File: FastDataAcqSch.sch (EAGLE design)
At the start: 94 parts, among them IC1 FT230XQ, J1 USB_MICROAB_SMT, X1 SMA-SMDRA, X2 87832-14, Y1 SI530-500

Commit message: Update 9/2/13
Added more ICs
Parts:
- added C62, C64, C66, C68: .1uF, Schuyler:CAPACITOR0204_REVERSE
- added C63, C65: 10nF, rcl:C-EUC0201
- added C67: 100pF, rcl:C-EUC0603
- added C69: 4.7uF, Schuyler:CAPACITOR0304_REVERSE
- added R19, R20, R24, R25: 10k, rcl:R-US_R0201
- added R21: 1k, rcl:R-US_0204/2V
- added R22: 83, rcl:R-US_0204/2V
- added R23: 130, rcl:R-US_0204/2V
- added U$6: TMP421, Schuyler:TMP421
- added U$7: DAC101C081, Schuyler:DAC101C081
- added Y2: DNP, Schuyler:SI500S
- added Y3: 100MHz, Schuyler:DS1088L_100MHZ
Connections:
- new net FPGA_CLK1: U$2.IO_L30N_GCLK0_USERCCLK_2, Y3.OUT
- new net FPGA_CLK2: U$2.IO_L31P_GCLK31_D14_2, Y2.OUTPUT
- new net FPGA_SCL: R19.1, R24.1, U$2.IO_L62N_D6_2, U$6.SCL, U$7.SCL
- new net FPGA_SDA: R20.1, R25.1, U$6.SDA, U$7.SDA
- new net FPGA_SDL: U$2.IO_L62P_D5_2
- new net N$10: R21.1
- new net N$9: R21.2, R22.2, R23.1
- new net VCC: R23.2
- net 3V3: now also C62.1, C63.1, C64.1, C65.1, C66.1, C68.1, C69.1, R19.2, R20.2, R24.2, R25.2, U$6.V+, U$7.VA, Y2.OE, Y2.VDD, Y3.!PDN, Y3.VCC@1, Y3.VCC@2
- net ADC_TDIODE+: now also C67.1, U$6.DXP
- net ADC_TDIODE-: now also C67.2, U$6.DXN
- net AGND: now also R22.1
- net DGND: now also C62.2, C63.2, C64.2, C65.2, C66.2, C68.2, C69.2, U$6.A0, U$6.A1, U$6.GND, U$7.ADR0, U$7.GND, Y2.GDN, Y3.GND@1, Y3.GND@2
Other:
- note added: "+"
- note added: "-"
- note added: "FPGA"
- note added: "FPGA Clock"
- note added: "Half of the differential output/differential latch input"
- note added: "Input Trigger"
- note added: "L"
- note added: "NOTE: C is 0603 so it can be changed"
- note added: "NOTE: Device address is: 1001 100"
- note added: "NOTE: Route CLK as 50 ohm impedance line. Termination described in datasheet."
- note added: "NOTE: Y3 is the primary clock. Y2 is a backup but should not be populated"
- note added: "Q"
- note added: "Temperature Sensor"
- note added: "Trigger"
- note added: "Trigger In"
- note added: "Trigger Reset"
- note added: "USB/UART Interface"
- note added: "Vref"
- note removed: "NOTE: Route CLK as 50 ohm impedance line."

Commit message: Nearly finalized schematic
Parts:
- removed R21: 1k, rcl:R-US_0204/2V
- removed R22: 83, rcl:R-US_0204/2V
- removed R23: 130, rcl:R-US_0204/2V
- removed R9: NA, rcl:R-US_R0603
- added C70, C71, C72, C73, C74, C75, C76, C77, C78, C97, C98, C99: 10uF, rcl:C-EUC0603
- added C79, C80, C81, C82, C83, C84, C85, C93: 33uF, SparkFun-Passives:CAP0805
- added C86, C87, C88, C89, C90, C91: 10pF, rcl:C-EUC0201
- added C92: 10nF, rcl:C-EUC0201
- added C94, C95, C96: 22uF 150mOhm ESR, rcl:C-USC0805
- added IC2: LT1963AEQ, linear-technology:LT1963AEQ
- added JP1: (no value), SparkFun-Passives:JUMPER-2PTH
- added L10, L11: 2.2uH, Schuyler:INDUCTOR_5.18X5.49
- added L6, L7, L8, L9: 2.2uH, Schuyler:INDUCTOR_3X3.6
- added R26, R27, R28, R29, R30, R31, R32, R33, R34, R35, R36, R37, R38, R41, R42, R43, R44, R45, R47, R48, R49: (no value), rcl:R-US_R0201
- added R39: 4.7k, rcl:R-US_R0201
- added R40: 0, rcl:R-US_R0603
- added R46, R50: (no value), rcl:R-US_R0603
- added R51: 10k, rcl:R-US_R0201
- added TP1, TP2, TP3, TP4, TP5, TP6, TP7, TP8, TP9: TPPAD1-13, testpad:TPPAD1-13
- added U$10: LT1963AEST-3.3, Schuyler:LT1963AEST-3.3
- added U$8: LTC3374QFN, Schuyler:LTC3374QFN
- added U$9: LT1963AEST-2.5, Schuyler:LT1963AEST-2.5
- R1: device rcl:R-US_R0402 -> rcl:R-US_R0201; MANPARTNUMBER (none) -> RC0603F49R9C; MANUFACTURER (none) -> Samsung Electro-Mechanics America, Inc; PARTNUMBER (none) -> 1276-3590-1-ND; SUPPLIER (none) -> DIGIKEY
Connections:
- removed net FGPA_PROGRAMB: U$2.PROGRAM_B_2
- removed net N$10: R21.1
- removed net N$9: R21.2, R22.2, R23.1
- new net 2V3_1V9PRE: C82.1, C89.1, C97.1, IC2.!SHDN, IC2.IN, L10.P$2, R32.2, TP3.TP
- new net 2V8_2V5PRE: C80.1, C91.1, C98.1, L9.P$2, R36.2, R48.2, TP1.TP, U$9.IN
- new net 3V3A: C96.1, L4.P$2, TP9.TP, U$10.OUT
- new net 3V6_PRE3V3: C84.1, C87.1, C99.1, L6.P$2, R28.2, TP5.TP, U$10.IN
- new net ADC_PWR_EN: R41.2, U$2.IO_L48P_D7_2, U$8G$5.EN
- new net ANALOG_PWR_EN: R47.2, U$2.IO_L48N_RDWR_B_VREF_2, U$8G$8.EN
- new net FPGA_PROGRAMB: R39.1, R40.2, U$2.PROGRAM_B_2
- new net N$11: R40.1, U$5.!CF
- new net N$12: R42.1, R43.2, U$8G$1.EN
- new net N$13: R44.1, R45.2, U$8G$4.EN
- new net N$14: IC2.SENSE, R46.1, R50.2
- new net N$16: R48.1, R49.2, U$8G$3.EN
- new net PGOOD: U$8G$9.PGOOD_ALL
- new net S1FB: C86.2, R26.1, R27.2, U$8G$1.FB
- new net S1SW: L11.P$1, U$8G$1.SW, U$8G$2.SW
- new net S3FB: C87.2, R28.1, R29.2, U$8G$3.FB
- new net S3SW: L6.P$1, U$8G$3.SW
- new net S4FB: C88.2, R30.1, R31.2, U$8G$4.FB
- new net S4SW: L7.P$1, U$8G$4.SW
- new net S5FB: C89.2, R32.1, R33.2, U$8G$5.FB
- new net S5SW: L10.P$1, U$8G$5.SW, U$8G$6.SW
- new net S7FB: C90.2, R34.1, R35.2, U$8G$7.FB
- new net S7SW: L8.P$1, U$8G$7.SW
- new net S8FB: C91.2, R36.1, R37.2, U$8G$8.FB
- new net S8SW: L9.P$1, U$8G$8.SW
- new net S_TEMP: U$8G$9.TEMP
- new net VIN: C70.1, C71.1, C72.1, C73.1, C74.1, C75.1, C76.1, C77.1, C78.1, C79.1, U$8G$1.VIN, U$8G$2.FB, U$8G$2.VIN, U$8G$3.VIN, U$8G$4.VIN, U$8G$5.VIN, U$8G$6.FB, U$8G$6.VIN, U$8G$7.EN, U$8G$7.VIN, U$8G$8.VIN, U$8G$9.RT, U$8G$9.VCC
- net 1V2: now also C81.1, C90.1, L8.P$2, R34.2, R42.2, TP2.TP
- net 1V8: now also C83.1, C88.1, L7.P$2, R30.2, TP4.TP
- net 1V9: now also C94.1, IC2.OUT, R46.2, TP7.TP
- net 1V9A: now also R51.2; no longer R9.2
- net 2V5: now also C95.1, TP8.TP, U$9.OUT
- net 3V3: now also C85.1, C86.1, C92.1, C93.1, L11.P$2, R26.2, R39.2, R44.2, TP6.TP; no longer L4.P$2
- net ADC_CALDLY/DES/!SCS: now also R51.1; no longer R9.1
- net AGND: now also R1.1; no longer R1.2, R22.1
- net DGND: now also C70.2, C71.2, C72.2, C73.2, C74.2, C75.2, C76.2, C77.2, C78.2, C79.2, C80.2, C81.2, C82.2, C83.2, C84.2, C85.2, C92.2, C93.2, C94.2, C95.2, C96.2, C97.2, C98.2, C99.2, IC2.GND, IC2.GND@1, R27.1, R29.1, R31.1, R33.1, R35.1, R37.1, R38.1, R41.1, R43.1, R45.1, R47.1, R49.1, R50.1, U$10.GND@1, U$10.GND@2, U$8G$2.EN, U$8G$6.EN, U$8G$9.GND, U$8G$9.SYNC, U$9.GND@1, U$9.GND@2
- net FPGA_CLK2: now also U$2.IO_L30P_GCLK1_D13_2; no longer U$2.IO_L31P_GCLK31_D14_2
- net N$2: now also R1.2; no longer R1.1
- net N$6: now also JP1.1, R38.2, U$8G$9.MODE; no longer U$2.IO_L1P_3
- net VCC: now also JP1.2; no longer R23.2
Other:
- note added: "FPGA & Digital Power"
- note added: "NOTE: !CF! used to by JTAG to reset FPGA. If wrong, desolder resistor."
- note added: "NOTE: ADC is initially in Power Down mode (PD/PDQ pulled high) and calibration delayed (ADC_CAL pulled high). When the FPGA is ready, it can begin the ADC power and calibration process."
- note added: "NOTE: Extra caps because Va is reference as well as power."
- note added: "Note: LDOs require >10mOhms ESR for stability and ringing damping."
- note added: "Note: Maybe make C bigger"
- note added: "Note: Ven is 420mV. Resistor divider should account for transient droop of at least 100mV."
- note added: "Power Regulation"
- note added: "Power Sequencing: 1) 1V2 supply is always enabled. 2) 3V3 enable once 1V2 is ready 3) 1V8 enabled once 3V3 is ready 4) ADC 1V9 enabled from FPGA 5) 2V5 and 3V3A enabled from FPGA. These shoud only be enabled after 1V9 is stable."
- note removed: "+"
- note removed: "-"
- note removed: "FPGA"
- note removed: "Half of the differential output/differential latch input"
- note removed: "L"
- note removed: "NOTE: !CF! used to by JTAG to reset FPGA. Leaving unconnected because feature not needed."
- note removed: "Q"
- note removed: "Trigger"
- note removed: "Trigger In"
- note removed: "Trigger Reset"
- note removed: "Vref"

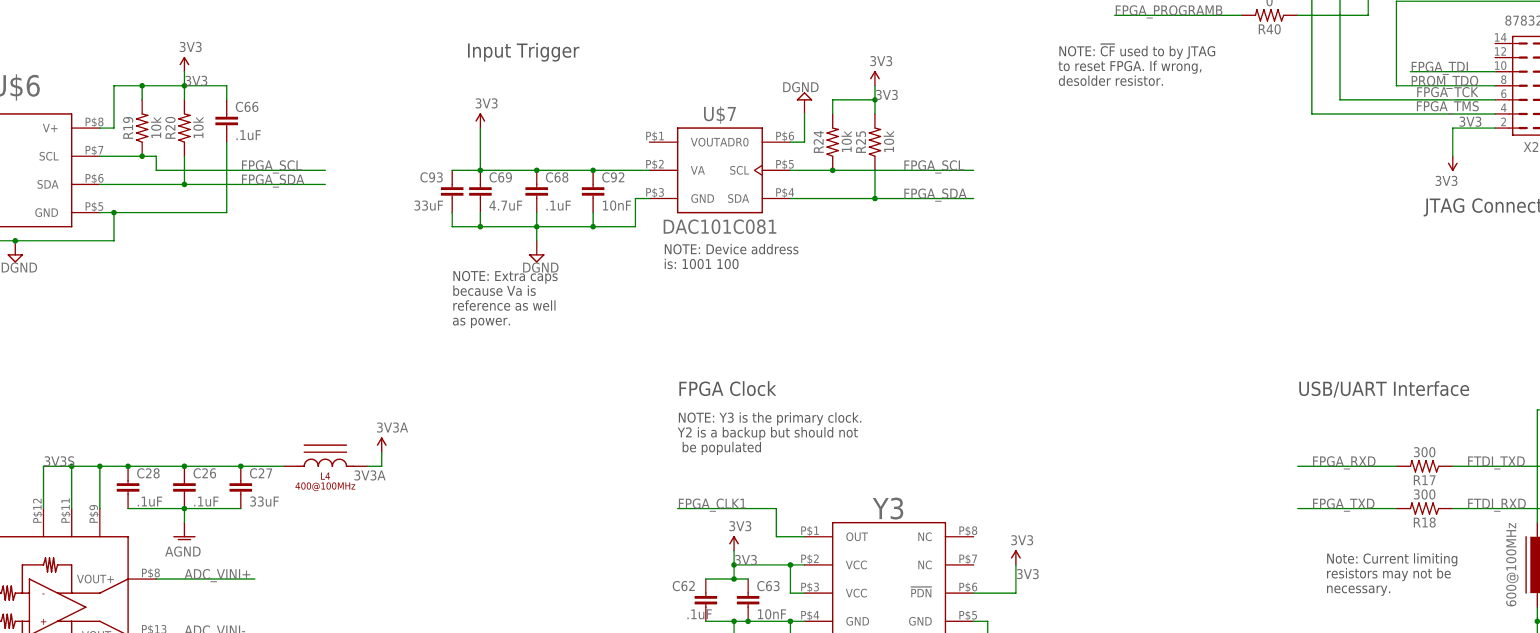
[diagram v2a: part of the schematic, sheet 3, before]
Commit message: Only 9 parts left to source
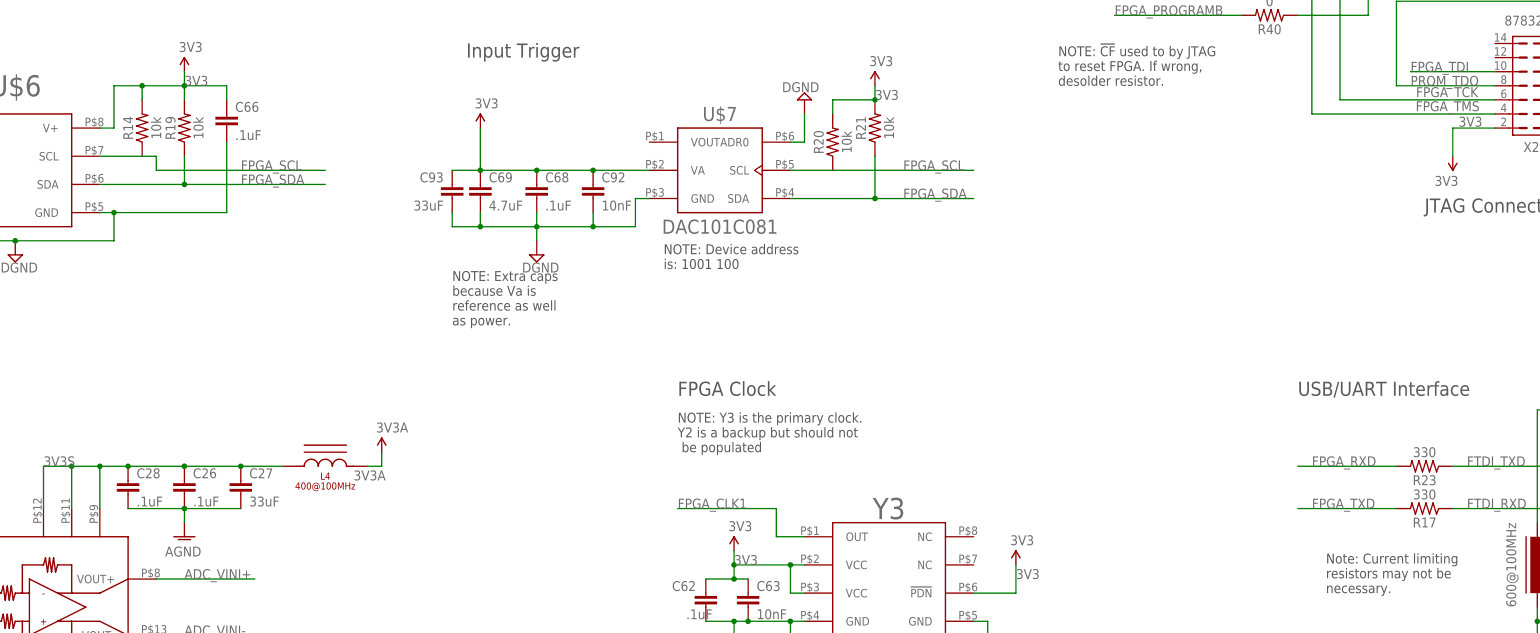
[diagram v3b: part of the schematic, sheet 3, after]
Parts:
- removed R18: 300, rcl:R-US_R0201
- removed R24, R25: 10k, rcl:R-US_R0201
- added R21, R9: 10k, rcl:R-US_R0201
- added R23: 330, rcl:R-US_R0201
- R13, R14, R19, R20, R22: MANPARTNUMBER (none) -> RC0603J103CS; MANUFACTURER (none) -> Samsung Electro-Mechanics America, Inc; PARTNUMBER (none) -> 1276-3817-1-ND; SUPPLIER (none) -> DIGIKEY
- R17: value 300 -> 330; MANPARTNUMBER (none) -> RC0603J331CS; MANUFACTURER (none) -> Samsung Electro-Mechanics America, Inc; PARTNUMBER P330AGCT-ND -> 1276-3787-1-ND
- R2: MANPARTNUMBER (none) -> RC0603J331CS; MANUFACTURER (none) -> Samsung Electro-Mechanics America, Inc; PARTNUMBER (none) -> 1276-3787-1-ND; SUPPLIER (none) -> DIGIKEY
- R26: value (none) -> 845k; PARTNUMBER (none) -> P845KABCT-ND; SUPPLIER (none) -> DIGIKEY
- R27: value (none) -> 270k; PARTNUMBER (none) -> P270KABCT-ND; SUPPLIER (none) -> DIGIKEY
- R28, R32, R36: value (none) -> 523K; PARTNUMBER (none) -> P523KABCT-ND; SUPPLIER (none) -> DIGIKEY
- R29: value (none) -> 150K; PARTNUMBER (none) -> 1276-3719-1-ND; SUPPLIER (none) -> DIGIKEY
- R3, R4: device rcl:R-US_R0201 -> rcl:R-US_R0402; MANPARTNUMBER (none) -> ERA-2AEB101X; MANUFACTURER (none) -> Panasonic Electronic Components; PARTNUMBER (none) -> P100DCCT-ND; SUPPLIER (none) -> DIGIKEY
- R30: value (none) -> 806K; PARTNUMBER (none) -> P806KABCT-ND; SUPPLIER (none) -> DIGIKEY
- R31: value (none) -> 649K; PARTNUMBER (none) -> P649KABCT-ND; SUPPLIER (none) -> DIGIKEY
- R33: value (none) -> 280K; PARTNUMBER (none) -> P280KABCT-ND; SUPPLIER (none) -> DIGIKEY
- R34, R37: value (none) -> 210K; PARTNUMBER (none) -> P210KABCT-ND; SUPPLIER (none) -> DIGIKEY
- R35: value (none) -> 422K; PARTNUMBER (none) -> P442KABCT-ND; SUPPLIER (none) -> DIGIKEY
- R46: value (none) -> 1.15k 1%; MANPARTNUMBER (none) -> RC1608F1151CS; MANUFACTURER (none) -> Samsung Electro-Mechanics America, Inc; PARTNUMBER (none) -> 1276-4649-1-ND; SUPPLIER (none) -> DIGIKEY
- R50: value (none) -> 2k 1%; MANPARTNUMBER (none) -> RC1608F202CS; MANUFACTURER (none) -> Samsung Electro-Mechanics America, Inc; PARTNUMBER (none) -> 1276-3495-1-ND; SUPPLIER (none) -> DIGIKEY
- R8: PARTNUMBER P3.3KDBCT-ND -> (none); SUPPLIER DIGIKEY -> (none)
- renumbered R51 to R22
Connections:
- net 1V9A: now also R9.1; no longer R14.1
- net 3V3: now also R21.2; no longer R20.2, R24.2, R25.2
- net ADC_CAL: now also R9.2; no longer R14.2
- net FPGA_RXD: now also R23.2; no longer R17.2
- net FPGA_SCL: no longer R19.1, R24.1
- net FPGA_SDA: now also R19.1, R21.1; no longer R20.1, R25.1
- net FPGA_TXD: now also R17.2; no longer R18.2
- net FTDI_RXD: now also R17.1; no longer R18.1
- net FTDI_TXD: now also R23.1; no longer R17.1
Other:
- moved on the sheet: R17, R19, R20, R35

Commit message: Schematic Finalized
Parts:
- added C100, C101: .1uF, Schuyler:CAPACITOR0204_REVERSE
- added C102: 4.7uF, Schuyler:CAPACITOR0304_REVERSE
- added IC3: ADCMP553BRMZ, Schuyler:ADCMP553BRMZ
- added R18, R24: 150K, rcl:R-US_R0201
- added R25: 210K, rcl:R-US_R0201
- added R51: 16k, rcl:R-US_R0603
- added R52, R53, R54: 50, rcl:R-US_R0201
- added R55: 100, rcl:R-US_R0603
- added X3: SMA-142-0701-801/806, con-coax:SMA-142-0701-801/806
- C1, C12, C13, C15, C17, C2, C4, C6, C7: value .1uF -> 10uF; device Schuyler:CAPACITOR0204_REVERSE -> rcl:C-EUC0603; PARTNUMBER 445-4061-1-ND -> 445-4112-1-ND
- C10, C11, C19, C3: value .1uF -> 33uF; device Schuyler:CAPACITOR0204_REVERSE -> SparkFun-Passives:CAP0805; PARTNUMBER 445-4061-1-ND -> 445-8238-1-ND; SUPPLIER DIGIKEY -> (none)
- C14, C8, C9: value .1uF -> 10pF; device Schuyler:CAPACITOR0204_REVERSE -> rcl:C-EUC0201; PARTNUMBER 445-4061-1-ND -> 445-1769-1-ND; SUPPLIER DIGIKEY -> (none)
- C16, C18, C5: value .1uF -> NA; device Schuyler:CAPACITOR0204_REVERSE -> rcl:C-EUC0603; PARTNUMBER 445-4061-1-ND -> (none); SUPPLIER DIGIKEY -> (none)
- C20, C21: value 33uF -> 10uF; device SparkFun-Passives:CAP0805 -> rcl:C-EUC0603; PARTNUMBER 445-8238-1-ND -> 445-4112-1-ND; SUPPLIER (none) -> DIGIKEY
- C22: value .1uF -> 10uF; device Schuyler:CAPACITOR0204_REVERSE -> rcl:C-EUC0603; PARTNUMBER 587-2152-1-ND -> 445-4112-1-ND
- C23: value 1uF -> 22uF 150mOhm ESR; device Schuyler:CAPACITOR0204_REVERSE -> rcl:C-USC0805; PARTNUMBER 445-9091-1-ND -> P16231CT-ND
- C24: value 4.7nF -> 22uF 150mOhm ESR; device rcl:C-EUC0201 -> rcl:C-USC0805; PARTNUMBER 445-1795-1-ND -> P16231CT-ND; SUPPLIER (none) -> DIGIKEY
- C25: value 4.7nF -> 10pF; PARTNUMBER 445-1795-1-ND -> 445-1769-1-ND
- C26: value .1uF -> 10pF; device Schuyler:CAPACITOR0204_REVERSE -> rcl:C-EUC0201; PARTNUMBER 587-2152-1-ND -> 445-1769-1-ND; SUPPLIER DIGIKEY -> (none)
- C27: value 33uF -> 10pF; device SparkFun-Passives:CAP0805 -> rcl:C-EUC0201; PARTNUMBER 445-8238-1-ND -> 445-1769-1-ND
- C28, C29: value .1uF -> 33uF; device Schuyler:CAPACITOR0204_REVERSE -> SparkFun-Passives:CAP0805; PARTNUMBER 587-2152-1-ND -> 445-8238-1-ND; SUPPLIER DIGIKEY -> (none)
- C30: value 0.47uF -> 33uF; device Schuyler:CAPACITOR0304_REVERSE -> SparkFun-Passives:CAP0805; PARTNUMBER 445-13744-1-ND -> 445-8238-1-ND; SUPPLIER DIGIKEY -> (none)
- C31: value 4.7uF -> 22uF 150mOhm ESR; device Schuyler:CAPACITOR0304_REVERSE -> rcl:C-USC0805; PARTNUMBER 445-13745-1-ND -> P16231CT-ND
- C36, C37, C42, C45, C56: value 4.7uF -> 0.47uF; PARTNUMBER 445-13745-1-ND -> 445-13744-1-ND
- C38, C39: value 4.7uF -> 33uF; device Schuyler:CAPACITOR0304_REVERSE -> SparkFun-Passives:CAP0805; PARTNUMBER 445-13745-1-ND -> 445-8238-1-ND; SUPPLIER DIGIKEY -> (none)
- C43, C44, C46, C47, C49, C53: value 0.47uF -> .1uF; device Schuyler:CAPACITOR0304_REVERSE -> Schuyler:CAPACITOR0204_REVERSE; PARTNUMBER 445-13744-1-ND -> 445-4061-1-ND
- C48, C69: value 4.7uF -> .1uF; device Schuyler:CAPACITOR0304_REVERSE -> Schuyler:CAPACITOR0204_REVERSE; PARTNUMBER 445-13745-1-ND -> 445-4061-1-ND
- C50, C52: value 0.47uF -> 4.7uF; PARTNUMBER 445-13744-1-ND -> 445-13745-1-ND
- C54, C58, C64, C66: PARTNUMBER 587-2152-1-ND -> 445-4061-1-ND
- C55: value 1uF -> 0.47uF; device Schuyler:CAPACITOR0204_REVERSE -> Schuyler:CAPACITOR0304_REVERSE; PARTNUMBER 445-9091-1-ND -> 445-13744-1-ND
- C57, C68: value .1uF -> 4.7uF; device Schuyler:CAPACITOR0204_REVERSE -> Schuyler:CAPACITOR0304_REVERSE; PARTNUMBER 587-2152-1-ND -> 445-13745-1-ND
- C59: value 47pF -> .1uF; device rcl:C-EUC0201 -> Schuyler:CAPACITOR0204_REVERSE; PARTNUMBER 445-1782-1-ND -> 445-4061-1-ND; SUPPLIER (none) -> DIGIKEY
- C60: value 47pF -> 4.7uF; device rcl:C-EUC0201 -> Schuyler:CAPACITOR0304_REVERSE; PARTNUMBER 445-1782-1-ND -> 445-13745-1-ND; SUPPLIER (none) -> DIGIKEY
- C61: value 10nF -> 0.47uF; device rcl:C-EUC0201 -> Schuyler:CAPACITOR0304_REVERSE; PARTNUMBER 445-1793-1-ND -> 445-13744-1-ND; SUPPLIER (none) -> DIGIKEY
- C62: value .1uF -> 0.47uF; device Schuyler:CAPACITOR0204_REVERSE -> Schuyler:CAPACITOR0304_REVERSE; PARTNUMBER 587-2152-1-ND -> 445-13744-1-ND
- C63: value 10nF -> .1uF; device rcl:C-EUC0201 -> Schuyler:CAPACITOR0204_REVERSE; PARTNUMBER 445-1793-1-ND -> 445-4061-1-ND; SUPPLIER (none) -> DIGIKEY
- C65: value 10nF -> 4.7uF; device rcl:C-EUC0201 -> Schuyler:CAPACITOR0304_REVERSE; PARTNUMBER 445-1793-1-ND -> 445-13745-1-ND; SUPPLIER (none) -> DIGIKEY
- C67: value 100pF -> .1uF; device rcl:C-EUC0603 -> Schuyler:CAPACITOR0204_REVERSE; PARTNUMBER 1276-1295-1-ND -> 445-4061-1-ND
- C70, C72, C73, C75: value 10uF -> .1uF; device rcl:C-EUC0603 -> Schuyler:CAPACITOR0204_REVERSE; PARTNUMBER 445-4112-1-ND -> 445-4061-1-ND
- C71, C74: value 10uF -> 4.7uF; device rcl:C-EUC0603 -> Schuyler:CAPACITOR0304_REVERSE; PARTNUMBER 445-4112-1-ND -> 445-13745-1-ND
- C76: value 10uF -> 0.47uF; device rcl:C-EUC0603 -> Schuyler:CAPACITOR0304_REVERSE; PARTNUMBER 445-4112-1-ND -> 445-13744-1-ND
- C77: value 10uF -> 100pF; PARTNUMBER 445-4112-1-ND -> 1276-1295-1-ND
- C78, C97: value 10uF -> .1uF; device rcl:C-EUC0603 -> Schuyler:CAPACITOR0204_REVERSE; PARTNUMBER 445-4112-1-ND -> 587-2152-1-ND
- C79, C82, C83, C85, C93: value 33uF -> .1uF; device SparkFun-Passives:CAP0805 -> Schuyler:CAPACITOR0204_REVERSE; PARTNUMBER 445-8238-1-ND -> 587-2152-1-ND; SUPPLIER (none) -> DIGIKEY
- C80, C81: value 33uF -> 4.7nF; device SparkFun-Passives:CAP0805 -> rcl:C-EUC0201; PARTNUMBER 445-8238-1-ND -> 445-1795-1-ND
- C86: value 10pF -> 1uF; device rcl:C-EUC0201 -> Schuyler:CAPACITOR0204_REVERSE; PARTNUMBER 445-1769-1-ND -> 445-9091-1-ND; SUPPLIER (none) -> DIGIKEY
- C87: value 10pF -> 33uF; device rcl:C-EUC0201 -> SparkFun-Passives:CAP0805; PARTNUMBER 445-1769-1-ND -> 445-8238-1-ND
- C88: value 10pF -> 4.7uF; device rcl:C-EUC0201 -> Schuyler:CAPACITOR0304_REVERSE; PARTNUMBER 445-1769-1-ND -> 445-13745-1-ND; SUPPLIER (none) -> DIGIKEY
- C89, C91: value 10pF -> .1uF; device rcl:C-EUC0201 -> Schuyler:CAPACITOR0204_REVERSE; PARTNUMBER 445-1769-1-ND -> 587-2152-1-ND; SUPPLIER (none) -> DIGIKEY
- C90: value 10pF -> 10nF; PARTNUMBER 445-1769-1-ND -> 445-1793-1-ND
- C94, C95: value 22uF 150mOhm ESR -> 10nF; device rcl:C-USC0805 -> rcl:C-EUC0201; PARTNUMBER P16231CT-ND -> 445-1793-1-ND; SUPPLIER DIGIKEY -> (none)
- C96: value 22uF 150mOhm ESR -> 47pF; device rcl:C-USC0805 -> rcl:C-EUC0201; PARTNUMBER P16231CT-ND -> 445-1782-1-ND; SUPPLIER DIGIKEY -> (none)
- C98: value 10uF -> 47pF; device rcl:C-EUC0603 -> rcl:C-EUC0201; PARTNUMBER 445-4112-1-ND -> 445-1782-1-ND; SUPPLIER DIGIKEY -> (none)
- C99: value 10uF -> 1uF; device rcl:C-EUC0603 -> Schuyler:CAPACITOR0204_REVERSE; PARTNUMBER 445-4112-1-ND -> 445-9091-1-ND
- IC1: value FT230XQ -> LT1963AEQ; device ftdichip:FT230XQ -> linear-technology:LT1963AEQ; MANPARTNUMBER (none) -> LT1963AEQ#PBF; MANUFACTURER (none) -> Linear Technology; PARTNUMBER (none) -> LT1963AEQ#PBF-ND; SUPPLIER (none) -> DIGIKEY
- IC2: value LT1963AEQ -> FT230XQ; device linear-technology:LT1963AEQ -> ftdichip:FT230XQ; MANPARTNUMBER LT1963AEQ#PBF -> (none); MANUFACTURER Linear Technology -> (none); PARTNUMBER LT1963AEQ#PBF-ND -> (none); SUPPLIER DIGIKEY -> (none)
- L1, L2, L4: value 400@100MHz -> 2.2uH; device Schuyler:FERRITE_BEADS2220 -> Schuyler:INDUCTOR_3X3.6; PARTNUMBER 445-6178-1-ND -> 541-1322-1-ND; SUPPLIER (none) -> DIGIKEY
- L10: value 2.2uH -> (none); device Schuyler:INDUCTOR_5.18X5.49 -> Schuyler:FERRITE_BEADS2220; PARTNUMBER 541-1220-1-ND -> (none); SUPPLIER DIGIKEY -> (none)
- L11: value 2.2uH -> 600@100MHz; device Schuyler:INDUCTOR_5.18X5.49 -> dp_devices:FERRITE-0603; PARTNUMBER 541-1220-1-ND -> 240-2371-1-ND
- L3: value (none) -> 2.2uH; device Schuyler:FERRITE_BEADS2220 -> Schuyler:INDUCTOR_5.18X5.49; PARTNUMBER (none) -> 541-1220-1-ND; SUPPLIER (none) -> DIGIKEY
- L5: value 600@100MHz -> 2.2uH; device dp_devices:FERRITE-0603 -> Schuyler:INDUCTOR_3X3.6; PARTNUMBER 240-2371-1-ND -> 541-1322-1-ND
- L6: device Schuyler:INDUCTOR_3X3.6 -> Schuyler:INDUCTOR_5.18X5.49; PARTNUMBER 541-1322-1-ND -> 541-1220-1-ND
- L7, L8, L9: value 2.2uH -> 400@100MHz; device Schuyler:INDUCTOR_3X3.6 -> Schuyler:FERRITE_BEADS2220; PARTNUMBER 541-1322-1-ND -> 445-6178-1-ND; SUPPLIER DIGIKEY -> (none)
- R1: value 50 -> NA; device rcl:R-US_R0201 -> rcl:R-US_R0603; MANPARTNUMBER RC0603F49R9C -> (none); MANUFACTURER Samsung Electro-Mechanics America, Inc -> (none); PARTNUMBER 1276-3590-1-ND -> (none); SUPPLIER DIGIKEY -> (none)
- R11: value NA -> 649K; device rcl:R-US_R0603 -> rcl:R-US_R0201; PARTNUMBER (none) -> P649KABCT-ND; SUPPLIER (none) -> DIGIKEY
- R12: value NA -> 150K; device rcl:R-US_R0603 -> rcl:R-US_R0201; PARTNUMBER (none) -> 1276-3719-1-ND; SUPPLIER (none) -> DIGIKEY
- R13: value 10k -> NA; device rcl:R-US_R0201 -> rcl:R-US_R0603; MANPARTNUMBER RC0603J103CS -> (none); MANUFACTURER Samsung Electro-Mechanics America, Inc -> (none); PARTNUMBER 1276-3817-1-ND -> (none); SUPPLIER DIGIKEY -> (none)
- R14, R19: value 10k -> 523K; MANPARTNUMBER RC0603J103CS -> (none); MANUFACTURER Samsung Electro-Mechanics America, Inc -> (none); PARTNUMBER 1276-3817-1-ND -> P523KABCT-ND
- R15, R16: value 27 -> 523K; PARTNUMBER 1276-3577-1-ND -> P523KABCT-ND
- R17: value 330 -> 210K; MANPARTNUMBER RC0603J331CS -> (none); MANUFACTURER Samsung Electro-Mechanics America, Inc -> (none); PARTNUMBER 1276-3787-1-ND -> P210KABCT-ND
- R2: value 330 -> NA; device rcl:R-US_R0201 -> rcl:R-US_R0603; MANPARTNUMBER RC0603J331CS -> (none); MANUFACTURER Samsung Electro-Mechanics America, Inc -> (none); PARTNUMBER 1276-3787-1-ND -> (none); SUPPLIER DIGIKEY -> (none)
- R20: value 10k -> 280K; MANPARTNUMBER RC0603J103CS -> (none); MANUFACTURER Samsung Electro-Mechanics America, Inc -> (none); PARTNUMBER 1276-3817-1-ND -> P280KABCT-ND
- R21: value 10k -> 270k; MANPARTNUMBER RC0603J103CS -> (none); MANUFACTURER Samsung Electro-Mechanics America, Inc -> (none); PARTNUMBER 1276-3817-1-ND -> P270KABCT-ND
- R22: value 10k -> 210K; MANPARTNUMBER RC0603J103CS -> (none); MANUFACTURER Samsung Electro-Mechanics America, Inc -> (none); PARTNUMBER 1276-3817-1-ND -> P210KABCT-ND
- R23: value 330 -> 806K; MANPARTNUMBER RC0603J331CS -> (none); MANUFACTURER Samsung Electro-Mechanics America, Inc -> (none); PARTNUMBER 1276-3787-1-ND -> P806KABCT-ND
- R26: value 845k -> 806K; PARTNUMBER P845KABCT-ND -> P806KABCT-ND
- R27: value 270k -> 845k; PARTNUMBER P270KABCT-ND -> P845KABCT-ND
- R28: value 523K -> 649K; PARTNUMBER P523KABCT-ND -> P649KABCT-ND
- R29: value 150K -> 422K; PARTNUMBER 1276-3719-1-ND -> P442KABCT-ND
- R3: value 100 0.1% -> NA; device rcl:R-US_R0402 -> rcl:R-US_R0603; MANPARTNUMBER ERA-2AEB101X -> (none); MANUFACTURER Panasonic Electronic Components -> (none); PARTNUMBER P100DCCT-ND -> (none); SUPPLIER DIGIKEY -> (none)
- R30: value 806K -> 270k; PARTNUMBER P806KABCT-ND -> P270KABCT-ND
- R31: value 649K -> 1.15k 1%; device rcl:R-US_R0201 -> rcl:R-US_R0603; MANPARTNUMBER (none) -> RC1608F1151CS; MANUFACTURER (none) -> Samsung Electro-Mechanics America, Inc; PARTNUMBER P649KABCT-ND -> 1276-4649-1-ND
- R32: value 523K -> 2k 1%; device rcl:R-US_R0201 -> rcl:R-US_R0603; MANPARTNUMBER (none) -> RC1608F202CS; MANUFACTURER (none) -> Samsung Electro-Mechanics America, Inc; PARTNUMBER P523KABCT-ND -> 1276-3495-1-ND
- R33: value 280K -> 50; MANPARTNUMBER (none) -> RC0603F49R9C; MANUFACTURER (none) -> Samsung Electro-Mechanics America, Inc; PARTNUMBER P280KABCT-ND -> 1276-3590-1-ND
- R34, R37: value 210K -> 10k; MANPARTNUMBER (none) -> RC0603J103CS; MANUFACTURER (none) -> Samsung Electro-Mechanics America, Inc; PARTNUMBER P210KABCT-ND -> 1276-3817-1-ND
- R35: value 422K -> 10k; MANPARTNUMBER (none) -> RC0603J103CS; MANUFACTURER (none) -> Samsung Electro-Mechanics America, Inc; PARTNUMBER P442KABCT-ND -> 1276-3817-1-ND
- R36: value 523K -> 10k; MANPARTNUMBER (none) -> RC0603J103CS; MANUFACTURER (none) -> Samsung Electro-Mechanics America, Inc; PARTNUMBER P523KABCT-ND -> 1276-3817-1-ND
- R38: value (none) -> NA; device rcl:R-US_R0201 -> rcl:R-US_R0603
- R39: value 4.7k -> 100 0.1%; device rcl:R-US_R0201 -> rcl:R-US_R0402; MANPARTNUMBER (none) -> ERA-2AEB101X; MANUFACTURER (none) -> Panasonic Electronic Components; PARTNUMBER (none) -> P100DCCT-ND; SUPPLIER (none) -> DIGIKEY
- R4: value 100 0.1% -> 10k; device rcl:R-US_R0402 -> rcl:R-US_R0201; MANPARTNUMBER ERA-2AEB101X -> RC0603J103CS; MANUFACTURER Panasonic Electronic Components -> Samsung Electro-Mechanics America, Inc; PARTNUMBER P100DCCT-ND -> 1276-3817-1-ND
- R40: value 0 -> 100 0.1%; device rcl:R-US_R0603 -> rcl:R-US_R0402; MANPARTNUMBER (none) -> ERA-2AEB101X; MANUFACTURER (none) -> Panasonic Electronic Components; PARTNUMBER 311-0.0GRCT-ND -> P100DCCT-ND
- R41, R44, R45: value (none) -> 330; MANPARTNUMBER (none) -> RC0603J331CS; MANUFACTURER (none) -> Samsung Electro-Mechanics America, Inc; PARTNUMBER (none) -> 1276-3787-1-ND; SUPPLIER (none) -> DIGIKEY
- R42: value (none) -> 4.7k
- R43: value (none) -> 0; device rcl:R-US_R0201 -> rcl:R-US_R0603; PARTNUMBER (none) -> 311-0.0GRCT-ND; SUPPLIER (none) -> DIGIKEY
- R46: value 1.15k 1% -> 27; device rcl:R-US_R0603 -> rcl:R-US_R0201; MANPARTNUMBER RC1608F1151CS -> (none); MANUFACTURER Samsung Electro-Mechanics America, Inc -> (none); PARTNUMBER 1276-4649-1-ND -> 1276-3577-1-ND
- R47: value (none) -> 27; PARTNUMBER (none) -> 1276-3577-1-ND; SUPPLIER (none) -> DIGIKEY
- R48: value (none) -> 10k; device rcl:R-US_R0201 -> rcl:R-US_R0603; PARTNUMBER (none) -> 311-0.0GRCT-ND; SUPPLIER (none) -> DIGIKEY
- R49: value (none) -> 26.1k; device rcl:R-US_R0201 -> rcl:R-US_R0603; PARTNUMBER (none) -> 311-0.0GRCT-ND; SUPPLIER (none) -> DIGIKEY
- R5: value 4.7k -> 10k; MANPARTNUMBER (none) -> RC0603J103CS; MANUFACTURER (none) -> Samsung Electro-Mechanics America, Inc; PARTNUMBER (none) -> 1276-3817-1-ND; SUPPLIER (none) -> DIGIKEY
- R50: value 2k 1% -> 10k; MANPARTNUMBER RC1608F202CS -> (none); MANUFACTURER Samsung Electro-Mechanics America, Inc -> (none); PARTNUMBER 1276-3495-1-ND -> 311-0.0GRCT-ND
- R6: value 3.3k 0.1% -> NA; PARTNUMBER P3.3KDBCT-ND -> (none); SUPPLIER DIGIKEY -> (none)
- R7: value NA -> 3.3k 0.1%; PARTNUMBER (none) -> P3.3KDBCT-ND; SUPPLIER (none) -> DIGIKEY
- R8: value NA -> 10k; device rcl:R-US_R0603 -> rcl:R-US_R0201; MANPARTNUMBER (none) -> RC0603J103CS; MANUFACTURER (none) -> Samsung Electro-Mechanics America, Inc; PARTNUMBER (none) -> 1276-3817-1-ND; SUPPLIER (none) -> DIGIKEY
- R9: value 10k -> 4.7k; MANPARTNUMBER RC0603J103CS -> (none); MANUFACTURER Samsung Electro-Mechanics America, Inc -> (none); PARTNUMBER 1276-3817-1-ND -> (none); SUPPLIER DIGIKEY -> (none)
- U$10: value LT1963AEST-3.3 -> XCFXXS04; device Schuyler:LT1963AEST-3.3 -> Schuyler:XCFXXS04
- U$3: value LMH6555 -> LTC3374QFN; device Schuyler:LMH6555 -> Schuyler:LTC3374QFN
- U$4: value LMV321SC-70 -> LT1963AEST-2.5; device Schuyler:LMV321SC-70 -> Schuyler:LT1963AEST-2.5
- U$5: value XCFXXS04 -> LT1963AEST-3.3; device Schuyler:XCFXXS04 -> Schuyler:LT1963AEST-3.3
- U$7: value DAC101C081 -> LMH6555; device Schuyler:DAC101C081 -> Schuyler:LMH6555
- U$8: value LTC3374QFN -> LMV321SC-70; device Schuyler:LTC3374QFN -> Schuyler:LMV321SC-70
- U$9: value LT1963AEST-2.5 -> DAC101C081; device Schuyler:LT1963AEST-2.5 -> Schuyler:DAC101C081
- X1: value SMA-SMDRA -> SMA-142-0701-801/806; device Schuyler:SMA-SMDRA -> con-coax:SMA-142-0701-801/806; MANPARTNUMBER (none) -> 142-0701-801; MANUFACTURER (none) -> Emerson Network Power Connectivity Johnson; PARTNUMBER (none) -> J502-ND; SUPPLIER (none) -> DIGIKEY
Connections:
- removed net CLK_500_ENABLE: Y1.OE
- removed net N$1: C22.1, C23.1, L3.P$1, Y1.VDD
- new net 2V5A: C85.1, C86.1, L10.P$1, Y1.OE, Y1.VDD
- new net FPGA_TRIG+: IC3.QA, R48.2, R53.2, U$2.IO_L31P_GCLK31_D14_2
- new net FPGA_TRIG-: IC3.!QA, R50.2, R52.2, U$2.IO_L31N_GCLK30_D15_2
- new net N$15: IC3.!LEA, R48.1, R49.2
- new net N$18: R52.1, R53.1, R54.2
- new net N$20: IC3.LEA, R50.1, R51.2
- new net TRIGGER: IC3.+IN_A, X1.1
- new net TRIG_REF: IC3.-IN_A, U$9.VOUT
- new net TRIG_RESET_HIGH: R51.1
- new net TRIG_RESET_LOW: R49.1
- net 1V2: now also C25.1, C28.1, C35.1, C40.1, C45.1, L4.P$2, R21.1, R25.2; no longer C30.1, C31.1, C33.1, C81.1, C90.1, L8.P$2, R34.2, R42.2
- net 1V8: now also C26.1, C29.1, L5.P$2, R26.2; no longer C83.1, C88.1, L7.P$2, R30.2
- net 1V9: now also C31.1, IC1.OUT, L7.P$1, L8.P$1, R31.2, R55.2; no longer C94.1, IC2.OUT, L1.P$1, L2.P$1, R46.2
- net 1V9A: now also C38.1, C43.1, C46.1, C48.1, C53.1, C58.1, C63.1, C66.1, C69.1, C72.1, C75.1, L7.P$2, R1.2, R4.1, R5.1, R6.2; no longer C1.1, C10.1, C2.1, C21.1, C3.1, C4.1, C5.1, C6.1, C7.1, C8.1, C9.1, L1.P$2, R11.2, R13.1, R22.2, R9.1
- net 1V9D: now also C39.1, C44.1, C47.1, C49.1, C54.1, C59.1, C64.1, C67.1, C70.1, C73.1, L8.P$2; no longer C11.1, C12.1, C13.1, C14.1, C15.1, C16.1, C17.1, C18.1, C19.1, C20.1, L2.P$2
- net 1V9F: now also C33.1, C36.1, C41.1, C50.1, C55.1, C56.1, C61.1, C62.1; no longer C42.1, C43.1, C44.1, C45.1, C46.1, C47.1, C52.1, C53.1
- net 2V3_1V9PRE: now also C14.1, C19.1, C22.1, IC1.!SHDN, IC1.IN, L3.P$2, R19.2; no longer C82.1, C89.1, C97.1, IC2.!SHDN, IC2.IN, L10.P$2, R32.2
- net 2V5: now also C23.1, L10.P$2, U$4.OUT; no longer C95.1, L3.P$2, U$9.OUT
- net 2V8_2V5PRE: now also C10.1, C20.1, C8.1, L1.P$2, R11.1, R15.2, U$4.IN; no longer C80.1, C91.1, C98.1, L9.P$2, R36.2, R48.2, U$9.IN
- net 3V3: now also C27.1, C30.1, C42.1, C52.1, C57.1, C60.1, C71.1, C74.1, C76.1, C83.1, C87.1, C88.1, C89.1, C90.1, C91.1, C94.1, C97.1, C99.1, IC3.VCC, L6.P$2, R23.2, R27.2, R35.2, R36.2, R37.2, R38.2, R41.2, R42.2, R9.2, U$10.VCCINT, U$10.VCCJ, U$10.VCCO, U$9.VA; no longer C35.1, C36.1, C38.1, C39.1, C40.1, C41.1, C48.1, C49.1, C50.1, C54.1, C55.1, C62.1, C63.1, C64.1, C66.1, C69.1, C85.1, C86.1, L11.P$2, R19.2, R2.2, R21.2, R26.2, R3.2, R44.2, R5.2, R7.2, U$5.VCCINT, U$5.VCCJ, U$5.VCCO, U$7.VA
- net 3V3A: now also C24.1, L9.P$2, U$5.OUT; no longer C96.1, L4.P$2, U$10.OUT
- net 3V3S: now also C78.1, C79.1, C82.1, C84.1, L9.P$1, U$7.VCC@1, U$7.VCC@2, U$7.VCC@3, U$8.V+; no longer C26.1, C27.1, C28.1, C29.1, L4.P$1, U$3.VCC@1, U$3.VCC@2, U$3.VCC@3, U$4.V+
- net 3V6_PRE3V3: now also C11.1, C21.1, C9.1, L2.P$2, R16.2, U$5.IN; no longer C84.1, C87.1, C99.1, L6.P$2, R28.2, U$10.IN
- net 5VUSB: now also C101.2, C102.1, IC2.VCC, L11.1; no longer C56.1, C57.2, IC1.VCC, L5.1
- net 5VUSB_CON: now also C95.1, L11.2; no longer C61.1, L5.2
- net ADC_CAL: now also R5.2; no longer R9.2
- net ADC_CALDLY/DES/!SCS: now also R8.1; no longer R22.1
- net ADC_CLK+: now also C80.2; no longer C24.2
- net ADC_CLK-: now also C81.2; no longer C25.2
- net ADC_DCLKRST: now also R3.2; no longer R12.2
- net ADC_FSR/ECE: now also R1.1, R2.2; no longer R10.2, R11.1
- net ADC_PD: now also R4.2; no longer R13.2
- net ADC_PWR_EN: now also R13.2, U$3G$5.EN; no longer R41.2, U$8G$5.EN
- net ADC_REXT: now also R7.2; no longer R6.2
- net ADC_TDIODE+: now also C77.1; no longer C67.1
- net ADC_TDIODE-: now also C77.2; no longer C67.2
- net ADC_VBG: now also R6.1; no longer R8.1
- net ADC_VCMO: now also U$8.+IN; no longer U$4.+IN
- net ADC_VCMO_BUFFER: now also U$7.VCM, U$8.-IN, U$8.VOUT; no longer U$3.VCM, U$4.-IN, U$4.VOUT
- net ADC_VINI+: now also U$7.VOUT+; no longer U$3.VOUT+
- net ADC_VINI-: now also U$7.VOUT-; no longer U$3.VOUT-
- net AGND: now also C38.2, C43.2, C46.2, C48.2, C53.2, C58.2, C63.2, C66.2, C69.2, C72.2, C75.2, C78.2, C79.2, C82.2, C84.2, C85.2, C86.2, R2.1, R3.1, R33.1, R7.1, U$7.GND@1, U$7.GND@2, U$7.GND@3, U$7.GND@4, U$7.GND@5, U$7.GND@6, U$7.GND@7, U$7.GND@8, U$7.XPAD, U$8.V-, X3.2; no longer C1.2, C10.2, C2.2, C21.2, C22.2, C23.2, C26.2, C27.2, C28.2, C29.2, C3.2, C4.2, C5.2, C6.2, C7.2, C8.2, C9.2, R1.1, R10.1, R12.1, R6.1, U$3.GND@1, U$3.GND@2, U$3.GND@3, U$3.GND@4, U$3.GND@5, U$3.GND@6, U$3.GND@7, U$3.GND@8, U$3.XPAD, U$4.V-, X1.2
- net ANALOG_PWR_EN: now also R10.2, U$3G$8.EN; no longer R47.2, U$8G$8.EN
- net CLK500+: now also C81.1; no longer C25.1
- net CLK500-: now also C80.1; no longer C24.1
- net DGND: now also C1.2, C10.2, C100.1, C101.1, C102.2, C2.2, C21.2, C22.2, C23.2, C24.2, C28.2, C29.2, C3.2, C4.2, C5.2, C57.2, C59.2, C6.2, C60.2, C67.2, C7.2, C87.2, C88.2, C89.2, C90.2, C91.2, C96.1, C98.1, IC1.GND@1, IC3.GND, R10.1, R12.2, R13.1, R14.1, R17.1, R18.1, R20.1, R22.1, R24.2, R28.1, R30.1, R32.1, R40.1, R54.1, R55.1, U$10.GND, U$3G$2.EN, U$3G$6.EN, U$3G$9.GND, U$3G$9.SYNC, U$4.GND@1, U$4.GND@2, U$5.GND@1, U$5.GND@2, U$9.ADR0, U$9.GND; no longer C14.2, C38.2, C43.2, C46.2, C48.2, C53.2, C57.1, C58.1, C59.1, C60.1, C63.2, C66.2, C69.2, C72.2, C75.2, C77.2, C78.2, C79.2, C80.2, C81.2, C82.2, C84.2, C85.2, C96.2, C98.2, IC2.GND@1, R27.1, R31.1, R33.1, R35.1, R37.1, R38.1, R4.1, R41.1, R43.1, R45.1, R47.1, R49.1, R50.1, U$10.GND@1, U$10.GND@2, U$5.GND, U$7.ADR0, U$7.GND, U$8G$2.EN, U$8G$6.EN, U$8G$9.GND, U$8G$9.SYNC, U$9.GND@1, U$9.GND@2
- net FPGA_CCLK: now also R38.1, R39.1, R40.2, U$10.CLK; no longer R3.1, R4.2, R7.1, U$5.CLK
- net FPGA_DIN: now also U$10.DO; no longer U$5.DO
- net FPGA_DONE: now also R41.1, U$10.!CE; no longer R2.1, U$5.!CE
- net FPGA_INITB: now also R42.1, U$10.OE/!RST; no longer R5.1, U$5.OE/!RST
- net FPGA_PROGRAMB: now also R43.2, R9.1; no longer R39.1, R40.2
- net FPGA_RXD: now also R44.2; no longer R23.2
- net FPGA_SCL: now also R36.1, U$9.SCL; no longer U$7.SCL
- net FPGA_SDA: now also R35.1, R37.1, U$9.SDA; no longer R19.1, R21.1, U$7.SDA
- net FPGA_TCK: now also U$10.TCK; no longer U$5.TCK
- net FPGA_TDO: now also U$10.TDI; no longer U$5.TDI
- net FPGA_TMS: now also U$10.TMS; no longer U$5.TMS
- net FPGA_TXD: now also R45.2; no longer R17.2
- net FTDI_RXD: now also IC2.RXD, R45.1; no longer IC1.RXD, R17.1
- net FTDI_TXD: now also IC2.TXD, R44.1; no longer IC1.TXD, R23.1
- net N$11: now also R43.1, U$10.!CF; no longer R40.1, U$5.!CF
- net N$12: now also C18.1, R21.2, R22.2, U$3G$1.EN; no longer R42.1, R43.2, U$8G$1.EN
- net N$13: now also C16.1, R23.1, R24.1, U$3G$4.EN; no longer R44.1, R45.2, U$8G$4.EN
- net N$14: now also IC1.SENSE, R31.1, R32.2; no longer IC2.SENSE, R46.1, R50.2
- net N$16: now also C5.1, R11.2, R12.1, U$3G$3.EN; no longer R48.1, R49.2, U$8G$3.EN
- net N$2: now also R33.2, U$7.VIN-; no longer R1.2, U$3.VIN-
- net N$3: now also IC2.USBDP, R46.2; no longer IC1.USBDP, R15.2
- net N$4: now also C96.2, R46.1; no longer C59.2, R15.1
- net N$5: now also C98.2, R47.1; no longer C60.2, R16.1
- net N$6: now also R14.2, U$3G$9.MODE; no longer R38.2, U$8G$9.MODE
- net N$7: now also IC2.USBDM, R47.2; no longer IC1.USBDM, R16.2
- net N$8: now also C100.2, IC2.!RESET, IC2.3V3OUT, IC2.VCCIO; no longer C58.2, IC1.!RESET, IC1.3V3OUT, IC1.VCCIO
- net PGOOD: now also U$3G$9.PGOOD_ALL; no longer U$8G$9.PGOOD_ALL
- net PROM_TDO: now also U$10.TDO; no longer U$5.TDO
- net S1FB: now also C27.2, R27.1, R30.2, U$3G$1.FB; no longer C86.2, R26.1, R27.2, U$8G$1.FB
- net S1SW: now also L6.P$1, U$3G$1.SW, U$3G$2.SW; no longer L11.P$1, U$8G$1.SW, U$8G$2.SW
- net S3FB: now also C9.2, R16.1, R18.2, U$3G$3.FB; no longer C87.2, R28.1, R29.2, U$8G$3.FB
- net S3SW: now also L2.P$1, U$3G$3.SW; no longer L6.P$1, U$8G$3.SW
- net S4FB: now also C26.2, R26.1, R28.2, U$3G$4.FB; no longer C88.2, R30.1, R31.2, U$8G$4.FB
- net S4SW: now also L5.P$1, U$3G$4.SW; no longer L7.P$1, U$8G$4.SW
- net S5FB: now also C14.2, R19.1, R20.2, U$3G$5.FB; no longer C89.2, R32.1, R33.2, U$8G$5.FB
- net S5SW: now also L3.P$1, U$3G$5.SW, U$3G$6.SW; no longer L10.P$1, U$8G$5.SW, U$8G$6.SW
- net S7FB: now also C25.2, R25.1, R29.2, U$3G$7.FB; no longer C90.2, R34.1, R35.2, U$8G$7.FB
- net S7SW: now also L4.P$1, U$3G$7.SW; no longer L8.P$1, U$8G$7.SW
- net S8FB: now also C8.2, R15.1, R17.2, U$3G$8.FB; no longer C91.2, R36.1, R37.2, U$8G$8.FB
- net S8SW: now also L1.P$1, U$3G$8.SW; no longer L9.P$1, U$8G$8.SW
- net SIGNAL_IN: now also U$7.VIN+, X3.1; no longer U$3.VIN+, X1.1
- net S_TEMP: now also U$3G$9.TEMP; no longer U$8G$9.TEMP
- net VIN: now also C1.1, C12.1, C13.1, C15.1, C17.1, C2.1, C3.1, C4.1, C6.1, C7.1, U$3G$1.VIN, U$3G$2.FB, U$3G$2.VIN, U$3G$3.VIN, U$3G$4.VIN, U$3G$5.VIN, U$3G$6.FB, U$3G$6.VIN, U$3G$7.EN, U$3G$7.VIN, U$3G$8.VIN, U$3G$9.RT, U$3G$9.VCC; no longer C70.1, C71.1, C72.1, C73.1, C74.1, C75.1, C76.1, C77.1, C78.1, C79.1, U$8G$1.VIN, U$8G$2.FB, U$8G$2.VIN, U$8G$3.VIN, U$8G$4.VIN, U$8G$5.VIN, U$8G$6.FB, U$8G$6.VIN, U$8G$7.EN, U$8G$7.VIN, U$8G$8.VIN, U$8G$9.RT, U$8G$9.VCC
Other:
- note added: "50 Ohm Transmission Lines"
- note added: "ADC and Analog Power"
- note added: "Additional Support ICs"
- note added: "LVPECL termination close to FPGA input pins."
- note added: "NOTE: Trig_Reset lines are normally tri-stated FPGA outputs. To reset the latch, they are simultanesoulsy brought high/low for 1 clock cycle."
- note added: "Note: 100 ohm resistor damps overshoot on power up. Recommended in ADC datasheet."
- note added: "Note: All differential pairs are routed as impedance controlled 100 ohm pairs (50 ohms individual impedance)."

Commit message: Changed Ferrites plus some peripherals
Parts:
- removed C67, C70, C73: .1uF, Schuyler:CAPACITOR0204_REVERSE
- added C103, C104, C105, C106, C107, C108: .1uF, Schuyler:CAPACITOR0204_REVERSE
- added J2: MICRO-FIT_3.0_2POS_RA_SMD, Schuyler:MICRO-FIT_3.0_2POS_RA_SMD
- added L12: CHOKE_CM_ACM7060-301, Schuyler:CHOKE_CM_ACM7060-301
- added L13: (no value), Schuyler:FERRITE_BEADS_BLM18SG260
- added U$11: SLIDER_SPDT_1101M2S3AQE2, Schuyler:SLIDER_SPDT_1101M2S3AQE2
- C109, C110, C111, C112, C43, C44, C46, C47, C48, C49, C53, C54, C58: PARTNUMBER 445-4061-1-ND -> 587-2152-1-ND
- C3: value 33uF -> 100uF; device SparkFun-Passives:CAP0805 -> Schuyler:CAP_POL_D9_SERIES; MANPARTNUMBER (none) -> ECASD91B107M012K00; PARTNUMBER 445-8238-1-ND -> 490-5480-1-ND
- C59, C64: value .1uF -> 10nF; device Schuyler:CAPACITOR0204_REVERSE -> rcl:C-EUC0201; PARTNUMBER 445-4061-1-ND -> 445-1793-1-ND; SUPPLIER DIGIKEY -> (none)
- C63: value .1uF -> 1uF; PARTNUMBER 445-4061-1-ND -> 445-9091-1-ND
- L10: device Schuyler:FERRITE_BEADS2220 -> Schuyler:FERRITE_BEADS_BLM18SG260
- L7, L8, L9: value 400@100MHz -> (none); device Schuyler:FERRITE_BEADS2220 -> Schuyler:FERRITE_BEADS_BLM18SG260; PARTNUMBER 445-6178-1-ND -> (none)
- R42, R9: MANPARTNUMBER (none) -> ERJ-1GNJ472C; MANUFACTURER (none) -> Panasonic Electronic Components; PARTNUMBER (none) -> P4.7AECT-ND; SUPPLIER (none) -> DIGIKEY
- renumbered C66 to C109, C69 to C110, C72 to C111, C75 to C112
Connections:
- new net N$1: L12.P$4, U$11.P$1
- new net N$17: C3.POS, L13.P$1, U$11.P$2
- new net POWER_IN+: J2.P$2, L12.P$1
- new net POWER_IN-: J2.P$1, L12.P$2
- net 1V9A: now also C103.1, C104.1, C105.1, C106.1, C107.1, C108.1; no longer C43.1, C46.1, C48.1, C53.1, C58.1, C63.1
- net 1V9D: now also C43.1, C46.1, C48.1, C53.1, C58.1; no longer C59.1, C64.1, C67.1, C70.1, C73.1
- net 2V5A: now also C64.1
- net 3V3: now also C59.1, C63.1; no longer R42.2
- net AGND: now also C103.2, C104.2, C105.2, C106.2, C107.2, C108.2, C64.2; no longer C43.2, C46.2, C48.2, C53.2, C58.2, C63.2
- net DGND: now also C3.NEG, C43.2, C46.2, C48.2, C53.2, C58.2, C63.2, L12.P$3, X1.2; no longer C3.2, C64.2, C67.2, C70.2, C73.2
- net FPGA_INITB: no longer R42.1
- net VIN: now also L13.P$2; no longer C3.1
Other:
- note removed: "Note: Maybe make C bigger"
- moved on the sheet: C12, C13, C15, C16, C17, C18, C25, C26, C27, C28, C29, C30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
